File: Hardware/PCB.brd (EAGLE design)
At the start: 170.2 x 111.2 mm, 103 parts, among them IC1 BD5229G-TR, IC4 XC6220A331MR-G, J1 FH34SRJ-24S-0.5SH_99_, J2 SAMACSYS_PARTS_USB4110-GF-A, J3 QWIIC_RIGHT_ANGLE, J4 112A-TAAR-R03_ATTEND, Q1 20V/4.2A/52mΩ/1.4W, Q2 20V/4.2A/52mΩ/1.4W, Q3 SI1308EDL-T1-GE3, U1 W25Q512JVEIQ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

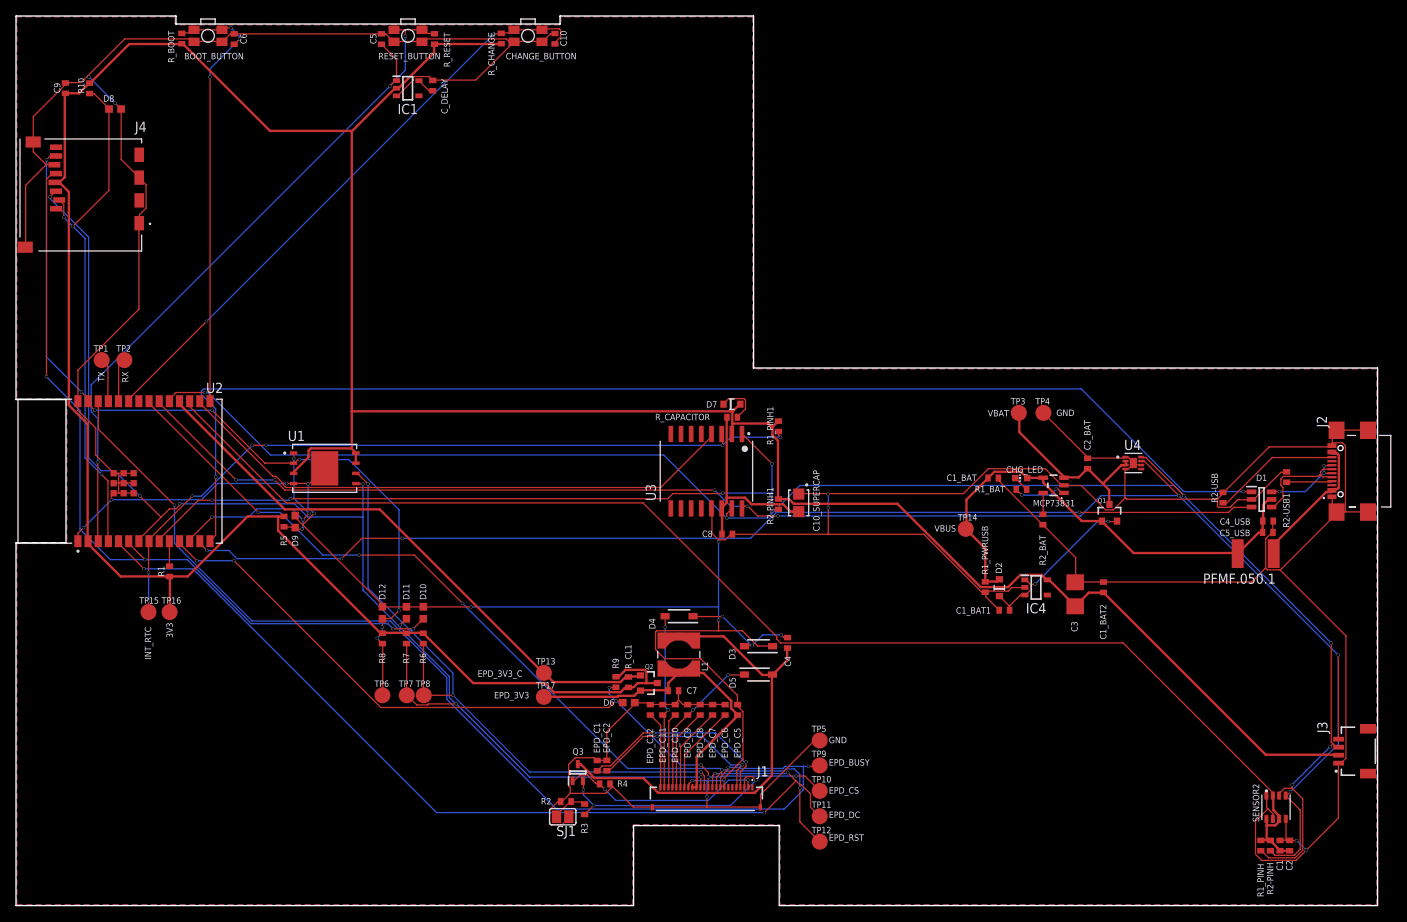
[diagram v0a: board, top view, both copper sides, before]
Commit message: Project update after the review
Upon receiving a review, i updated my project to fix the signaled issues:
- 90 degrees wires were eliminated
- measurements around the board were added
- the silkscreen has been cleared and enhanced to not intersect with the wires or the components
- the ground plane is not covering the entire surface of both the TOP and BOTTOM layer
- the board has now the correct 1mm width
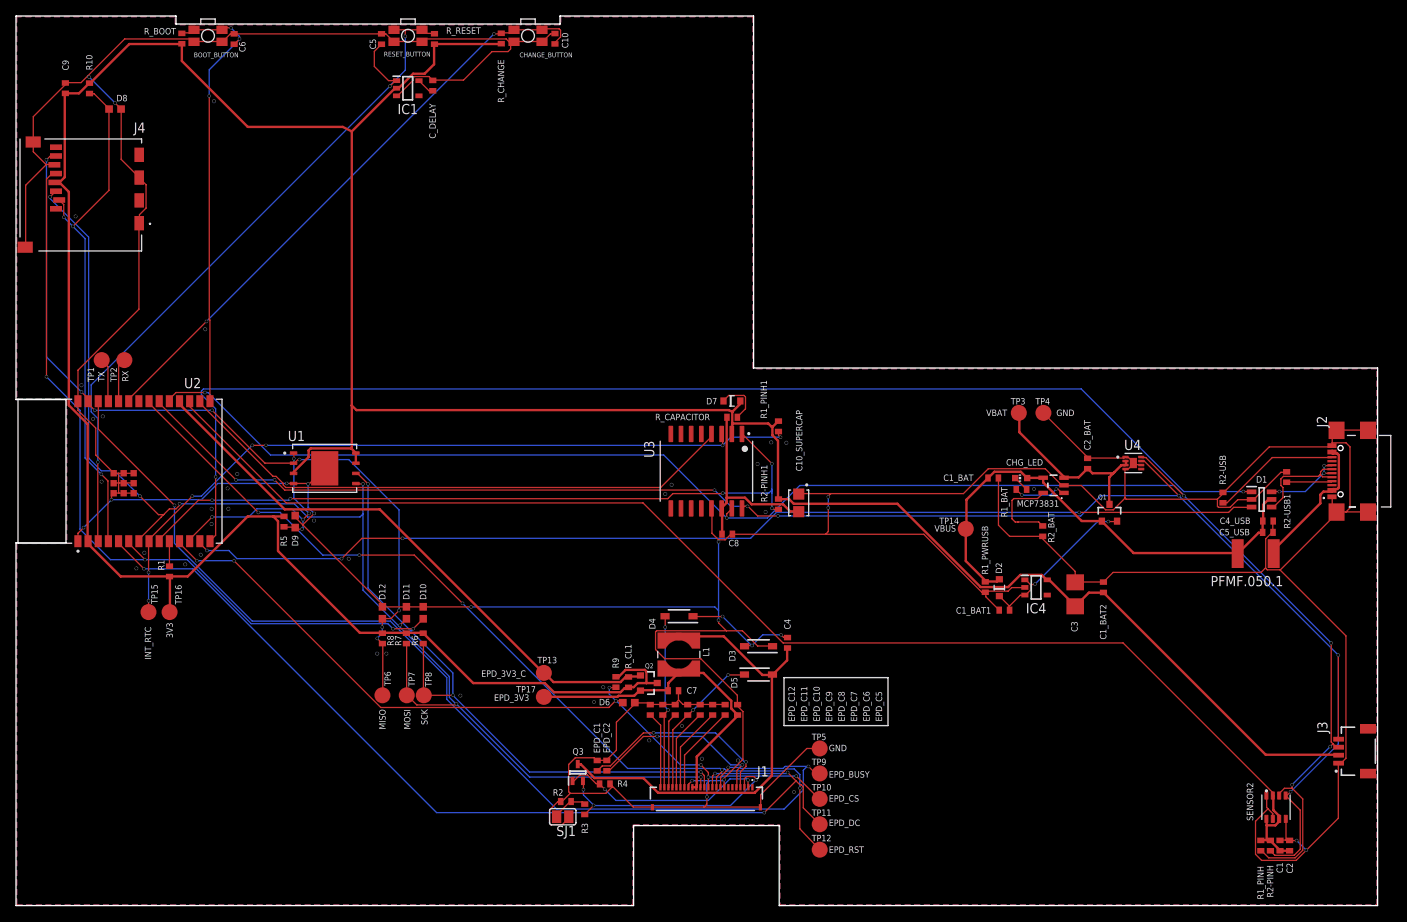
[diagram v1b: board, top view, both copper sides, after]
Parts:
- moved R2_BAT 1.45 mm to (128.3, 46.8)
- moved TP10 1.00 mm to (100.5, 13.3)
- moved TP11 1.00 mm to (100.5, 10.2)
- moved TP12 1.00 mm to (100.5, 6.99)
- moved TP5 1.00 mm to (100.5, 19.6)
- moved TP9 1.00 mm to (100.5, 16.5)
- moved D7 0.40 mm to (89.5, 63.1)
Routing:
- net N$6: track 2.68 -> 10.8 mm
- net 3V3: track 427.8 -> 432.2 mm
- net GND: track 723.0 -> 727.0 mm, vias 17 -> 52
- net RESET: track 92.3 -> 93.7 mm
- net EPD_RST: track 112.9 -> 114.0 mm
- net EPD_DC: track 118.8 -> 119.8 mm
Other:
- board text added: "MISO"
- board text added: "MOSI"
- board text added: "SCK"
